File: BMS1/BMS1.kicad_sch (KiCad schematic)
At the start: 75 parts, among them J1 Conn_01x02, J2 Conn_01x02, J3 Conn_01x02, Q2 DXT5551P5-13_DIO, Q3 DXT5551P5-13_DIO, T1 ESMIT-4180_C, U1 ADG728, U10 LTC6812-1, U2 ADG728, U3 ADG728, U4 ADG728, U5 ADG728, U6 ADG728, U7 ADG728, U8 ADG728, U9 LTC6812-1

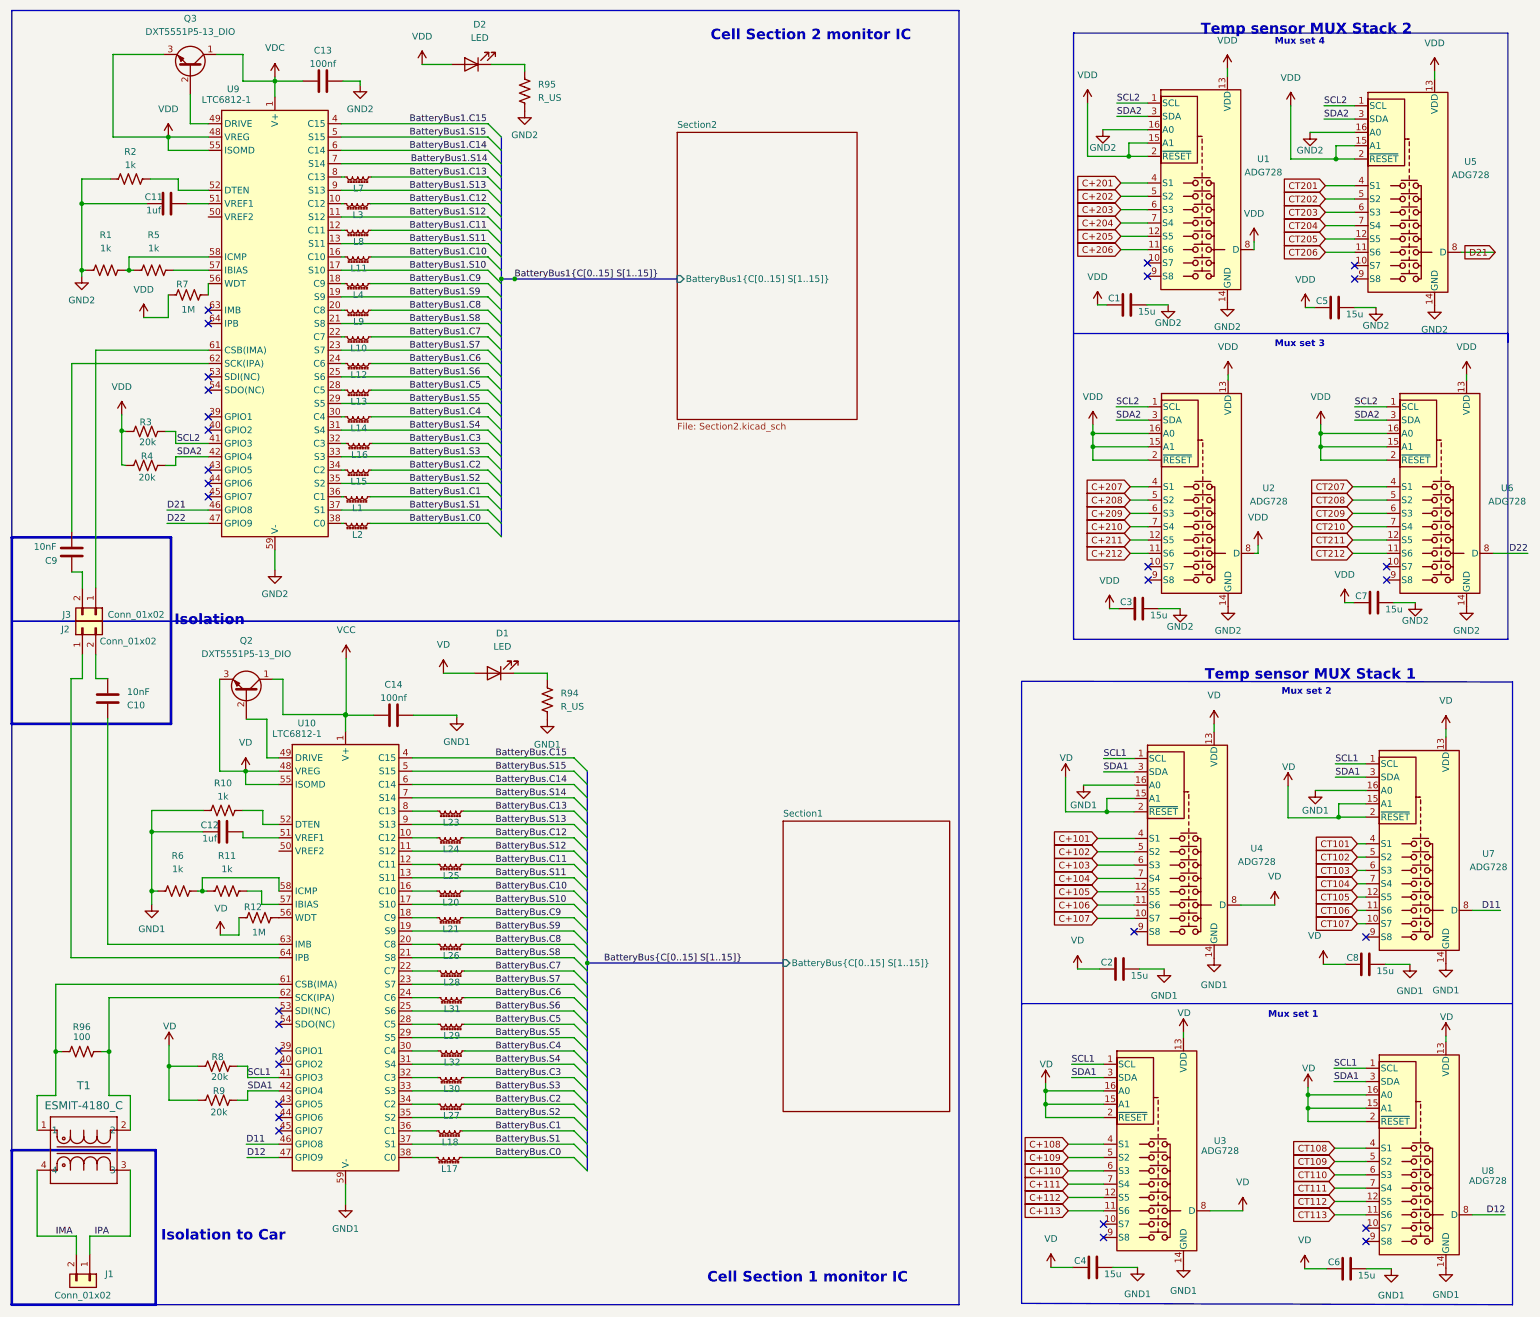
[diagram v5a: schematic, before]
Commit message: fixed to whats on board footy not changed
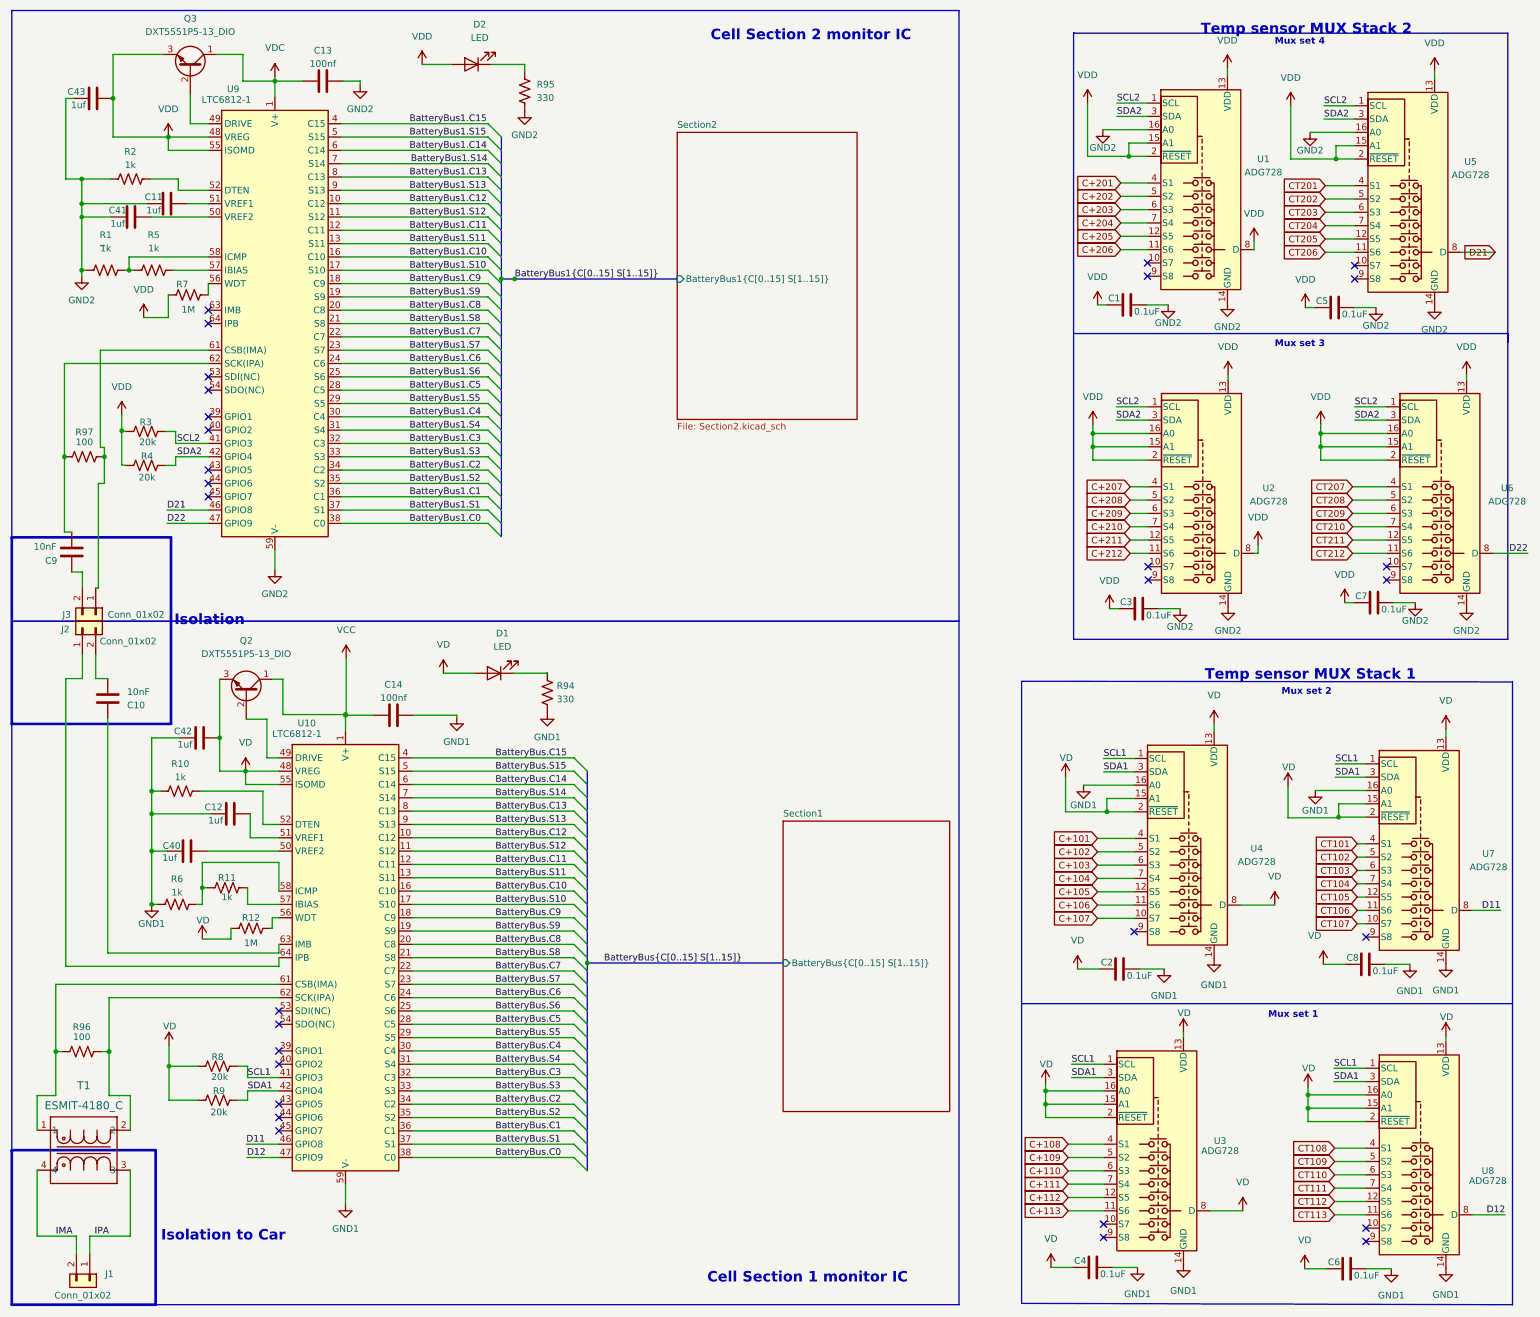
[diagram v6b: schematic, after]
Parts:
- removed L1, L10, L11, L12, L13, L14, L15, L16, L17, L18, L2, L20, L21, L23, L24, L25, L26, L27, L28, L29, L3, L30, L31, L32, L4, L7, L8, L9: L_Ferrite_Small, Inductor_SMD:L_0603_1608Metric_Pad1.05x0.95mm_HandSolder, symbol Device:L_Ferrite_Small
- added C40: 1uf, symbol Device:C
- added C41, C42, C43: 1uf, Capacitor_SMD:C_0603_1608Metric_Pad1.08x0.95mm_HandSolder, symbol Device:C
- added R97: 100, symbol Device:R_US
- C1, C2, C3, C4, C5, C6, C7, C8: value 15u -> 0.1uF
- R94, R95: value R_US -> 330
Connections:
- net BatteryBus.C0: now also U10.38 (C0)
- net BatteryBus.C1: now also U10.36 (C1)
- net BatteryBus.C10: now also U10.16 (C10)
- net BatteryBus.C11: now also U10.12 (C11)
- net BatteryBus.C12: now also U10.10 (C12)
- net BatteryBus.C13: now also U10.8 (C13)
- net BatteryBus.C2: now also U10.34 (C2)
- net BatteryBus.C3: now also U10.32 (C3)
- net BatteryBus.C4: now also U10.30 (C4)
- net BatteryBus.C5: now also U10.28 (C5)
- net BatteryBus.C6: now also U10.24 (C6)
- net BatteryBus.C7: now also U10.22 (C7)
- net BatteryBus.C8: now also U10.20 (C8)
- net BatteryBus.C9: now also U10.18 (C9)
- net BatteryBus1.C0: now also U9.38 (C0)
- net BatteryBus1.C1: now also U9.36 (C1)
- net BatteryBus1.C10: now also U9.16 (C10)
- net BatteryBus1.C11: now also U9.12 (C11)
- net BatteryBus1.C12: now also U9.10 (C12)
- net BatteryBus1.C13: now also U9.8 (C13)
- net BatteryBus1.C2: now also U9.34 (C2)
- net BatteryBus1.C3: now also U9.32 (C3)
- net BatteryBus1.C4: now also U9.30 (C4)
- net BatteryBus1.C5: now also U9.28 (C5)
- net BatteryBus1.C6: now also U9.24 (C6)
- net BatteryBus1.C7: now also U9.22 (C7)
- net BatteryBus1.C8: now also U9.20 (C8)
- net BatteryBus1.C9: now also U9.18 (C9)
- net GND1: now also C40.1, C42.1
- net GND2: now also C41.1, C43.1
- net VD: now also C42.2
- net VDD: now also C43.2
- net at C9.1, U9.62 (SCK(IPA)): now also R97.1
- net at U10.50 (VREF2): now also C40.2
- net at J3.1 (Pin_1), U9.61 (CSB(IMA)): now also R97.2
- net at U9.50 (VREF2): now also C41.2
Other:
- moved on the sheet: C12, R10, R11, R12, R6, R94
